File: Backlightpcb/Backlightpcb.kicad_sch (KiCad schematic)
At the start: 28 parts

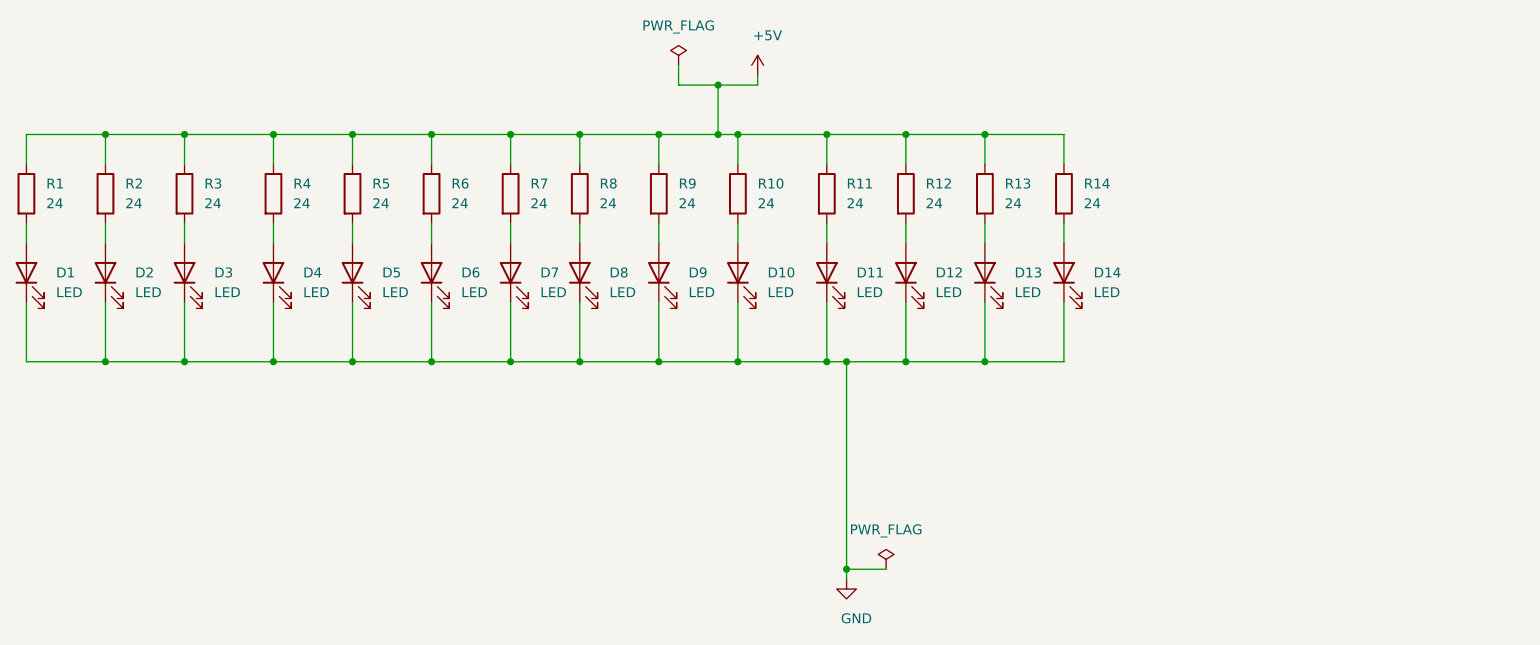
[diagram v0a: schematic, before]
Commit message: GND Zone
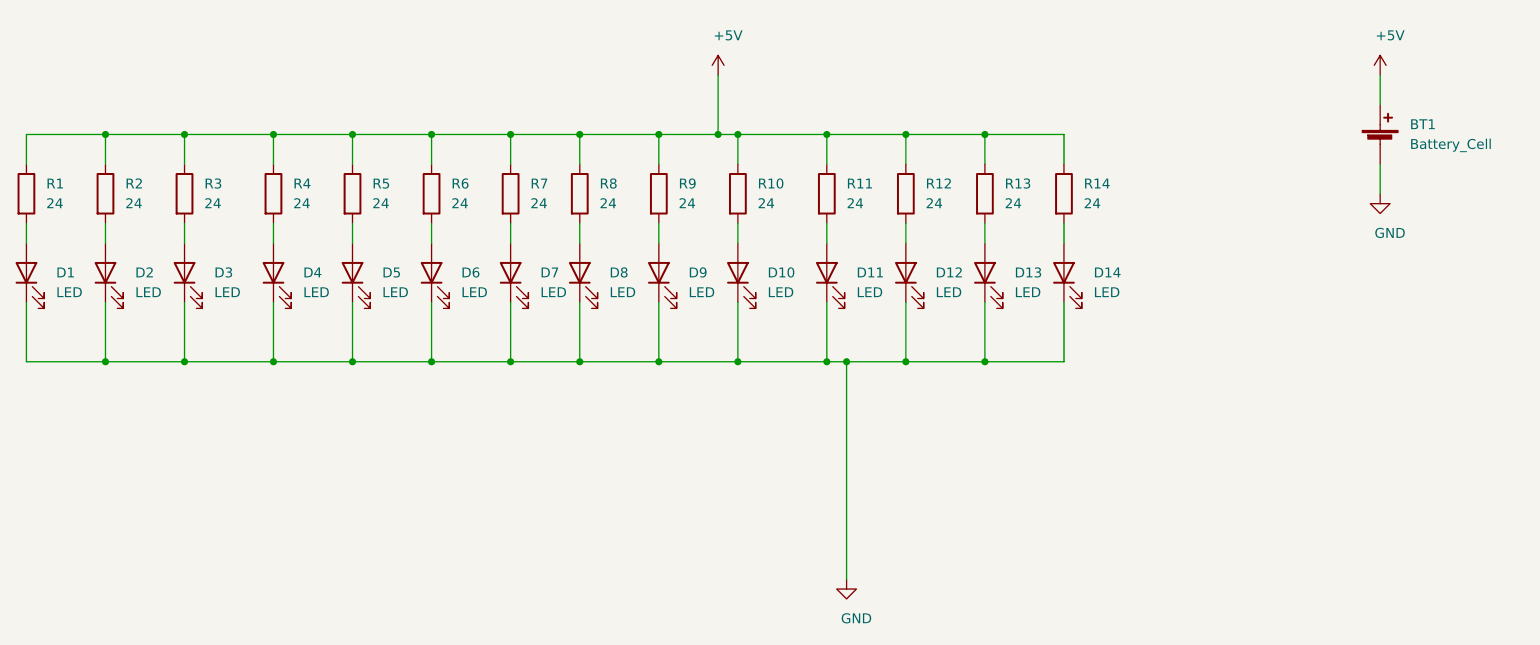
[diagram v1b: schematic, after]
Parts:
- added BT1: Battery_Cell, Connector_Wire:SolderWire-0.5sqmm_1x02_P4.6mm_D0.9mm_OD2.1mm, symbol Device:Battery_Cell
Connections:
- net +5V: now also BT1.1 (+)
- net GND: now also BT1.2 (-)
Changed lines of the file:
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@@
   (junction (at 125.73 86.36) (diameter 0.9144) (color 0 0 0 0))
   (junction (at 125.73 115.57) (diameter 0.9144) (color 0 0 0 0))
-  (junction (at 133.35 80.01) (diameter 0.9144) (color 0 0 0 0))
   (junction (at 133.35 86.36) (diameter 0.9144) (color 0 0 0 0))
   (junction (at 135.89 86.36) (diameter 0.9144) (color 0 0 0 0))
@@
   (junction (at 147.32 115.57) (diameter 0.9144) (color 0 0 0 0))
   (junction (at 149.86 115.57) (diameter 0.9144) (color 0 0 0 0))
-  (junction (at 149.86 142.24) (diameter 0.9144) (color 0 0 0 0))
   (junction (at 157.48 86.36) (diameter 0.9144) (color 0 0 0 0))
   (junction (at 157.48 115.57) (diameter 0.9144) (color 0 0 0 0))
@@
     (stroke (width 0) (type solid) (color 0 0 0 0))
   )
-  (wire (pts (xy 128.27 77.47) (xy 128.27 80.01))
-    (stroke (width 0) (type solid) (color 0 0 0 0))
-  )
-  (wire (pts (xy 128.27 80.01) (xy 133.35 80.01))
-    (stroke (width 0) (type solid) (color 0 0 0 0))
-  )
-  (wire (pts (xy 133.35 80.01) (xy 133.35 86.36))
-    (stroke (width 0) (type solid) (color 0 0 0 0))
-  )
-  (wire (pts (xy 133.35 80.01) (xy 138.43 80.01))
+  (wire (pts (xy 133.35 78.74) (xy 133.35 86.36))
     (stroke (width 0) (type solid) (color 0 0 0 0))
   )
@@
     (stroke (width 0) (type solid) (color 0 0 0 0))
   )
-  (wire (pts (xy 138.43 78.74) (xy 138.43 80.01))
-    (stroke (width 0) (type solid) (color 0 0 0 0))
-  )
   (wire (pts (xy 147.32 86.36) (xy 147.32 90.17))
     (stroke (width 0) (type solid) (color 0 0 0 0))
@@
     (stroke (width 0) (type solid) (color 0 0 0 0))
   )
-  (wire (pts (xy 149.86 115.57) (xy 149.86 142.24))
-    (stroke (width 0) (type solid) (color 0 0 0 0))
-  )
-  (wire (pts (xy 149.86 142.24) (xy 149.86 143.51))
-    (stroke (width 0) (type solid) (color 0 0 0 0))
-  )
-  (wire (pts (xy 149.86 142.24) (xy 154.94 142.24))
+  (wire (pts (xy 149.86 115.57) (xy 149.86 143.51))
     (stroke (width 0) (type solid) (color 0 0 0 0))
   )
@@
     (stroke (width 0) (type solid) (color 0 0 0 0))
   )
-  (symbol (lib_id "power:PWR_FLAG") (at 128.27 77.47 0) (unit 1)
-    (in_bom yes) (on_board yes)
-    (property "Reference" "#FLG01" (id 0) (at 128.27 75.565 0)
-      (effects (font (size 1.27 1.27)) hide)
-    )
-    (property "Value" "PWR_FLAG" (id 1) (at 128.27 72.39 0))
-    (property "Footprint" "" (id 2) (at 128.27 77.47 0)
-      (effects (font (size 1.27 1.27)) hide)
-    )
-    (property "Datasheet" "~" (id 3) (at 128.27 77.47 0)
-      (effects (font (size 1.27 1.27)) hide)
-    )
-  )
-  (symbol (lib_id "power:PWR_FLAG") (at 154.94 142.24 0) (unit 1)
-    (in_bom yes) (on_board yes)
-    (property "Reference" "#FLG02" (id 0) (at 154.94 140.335 0)
-      (effects (font (size 1.27 1.27)) hide)
-    )
-    (property "Value" "PWR_FLAG" (id 1) (at 154.94 137.16 0))
-    (property "Footprint" "" (id 2) (at 154.94 142.24 0)
-      (effects (font (size 1.27 1.27)) hide)
-    )
-    (property "Datasheet" "~" (id 3) (at 154.94 142.24 0)
-      (effects (font (size 1.27 1.27)) hide)
-    )
-  )
-  (symbol (lib_id "power:+5V") (at 138.43 78.74 0) (unit 1)
-    (in_bom yes) (on_board yes)
-    (property "Reference" "#PWR01" (id 0) (at 138.43 82.55 0)
-      (effects (font (size 1.27 1.27)) hide)
-    )
-    (property "Value" "+5V" (id 1) (at 139.7 73.66 0))
-    (property "Footprint" "" (id 2) (at 138.43 78.74 0)
-      (effects (font (size 1.27 1.27)) hide)
-    )
-    (property "Datasheet" "" (id 3) (at 138.43 78.74 0)
+  (wire (pts (xy 218.44 78.74) (xy 218.44 82.55))
+    (stroke (width 0) (type solid) (color 0 0 0 0))
+  )
+  (wire (pts (xy 218.44 90.17) (xy 218.44 93.98))
+    (stroke (width 0) (type solid) (color 0 0 0 0))
+  )
+  (symbol (lib_id "power:+5V") (at 133.35 78.74 0) (unit 1)
+    (in_bom yes) (on_board yes)
+    (property "Reference" "#PWR01" (id 0) (at 133.35 82.55 0)
+      (effects (font (size 1.27 1.27)) hide)
+    )
+    (property "Value" "+5V" (id 1) (at 134.62 73.66 0))
+    (property "Footprint" "" (id 2) (at 133.35 78.74 0)
+      (effects (font (size 1.27 1.27)) hide)
+    )
+    (property "Datasheet" "" (id 3) (at 133.35 78.74 0)
+      (effects (font (size 1.27 1.27)) hide)
+    )
+  )
+  (symbol (lib_id "power:+5V") (at 218.44 78.74 0) (unit 1)
+    (in_bom yes) (on_board yes)
+    (property "Reference" "#PWR0101" (id 0) (at 218.44 82.55 0)
+      (effects (font (size 1.27 1.27)) hide)
+    )
+    (property "Value" "+5V" (id 1) (at 219.71 73.66 0))
+    (property "Footprint" "" (id 2) (at 218.44 78.74 0)
+      (effects (font (size 1.27 1.27)) hide)
+    )
+    (property "Datasheet" "" (id 3) (at 218.44 78.74 0)
       (effects (font (size 1.27 1.27)) hide)
     )
@@
     )
   )
+  (symbol (lib_id "power:GND") (at 218.44 93.98 0) (unit 1)
+    (in_bom yes) (on_board yes)
+    (property "Reference" "#PWR0102" (id 0) (at 218.44 100.33 0)
+      (effects (font (size 1.27 1.27)) hide)
+    )
+    (property "Value" "GND" (id 1) (at 219.71 99.06 0))
+    (property "Footprint" "" (id 2) (at 218.44 93.98 0)
+      (effects (font (size 1.27 1.27)) hide)
+    )
+    (property "Datasheet" "" (id 3) (at 218.44 93.98 0)
+      (effects (font (size 1.27 1.27)) hide)
+    )
+  )
   (symbol (lib_id "Device:R") (at 44.45 93.98 0) (unit 1)
     (in_bom yes) (on_board yes)
@@
     )
     (property "Datasheet" "~" (id 3) (at 177.8 104.14 0)
+      (effects (font (size 1.27 1.27)) hide)
+    )
+  )
+  (symbol (lib_id "Device:Battery_Cell") (at 218.44 87.63 0) (unit 1)
+    (in_bom yes) (on_board yes)
+    (property "Reference" "BT1" (id 0) (at 222.25 85.09 0)
+      (effects (font (size 1.27 1.27)) (justify left))
+    )
+    (property "Value" "Battery_Cell" (id 1) (at 222.25 87.63 0)
+      (effects (font (size 1.27 1.27)) (justify left))
+    )
+    (property "Footprint" "Connector_Wire:SolderWire-0.5sqmm_1x02_P4.6mm_D0.9mm_OD2.1mm" (id 2) (at 218.44 86.106 90)
+      (effects (font (size 1.27 1.27)) hide)
+    )
+    (property "Datasheet" "~" (id 3) (at 218.44 86.106 90)
       (effects (font (size 1.27 1.27)) hide)
     )
@@
   )
   (symbol_instances
-    (path "/33924d3d-6f94-44ca-a859-88f507ac0e24"
-      (reference "#FLG01") (unit 1) (value "PWR_FLAG") (footprint "")
-    )
-    (path "/ceeb3b1d-3f28-4c2b-861a-f83f34a6efc2"
-      (reference "#FLG02") (unit 1) (value "PWR_FLAG") (footprint "")
-    )
     (path "/deed03ae-f04e-4410-aa4c-bf50338ea4b2"
       (reference "#PWR01") (unit 1) (value "+5V") (footprint "")
@@
       (reference "#PWR02") (unit 1) (value "GND") (footprint "")
     )
+    (path "/edd3ccd2-de8a-434c-aa98-200495296cfd"
+      (reference "#PWR0101") (unit 1) (value "+5V") (footprint "")
+    )
+    (path "/c3ff94c3-8671-4251-8ca8-2b9a1ebae203"
+      (reference "#PWR0102") (unit 1) (value "GND") (footprint "")
+    )
+    (path "/8424665a-0221-436e-81cc-723e1e61ee79"
+      (reference "BT1") (unit 1) (value "Battery_Cell") (footprint "Connector_Wire:SolderWire-0.5sqmm_1x02_P4.6mm_D0.9mm_OD2.1mm")
+    )
     (path "/853f341a-66b1-42e4-bad0-df0ab926471a"
